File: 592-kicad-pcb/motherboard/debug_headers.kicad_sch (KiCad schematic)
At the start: 0 parts

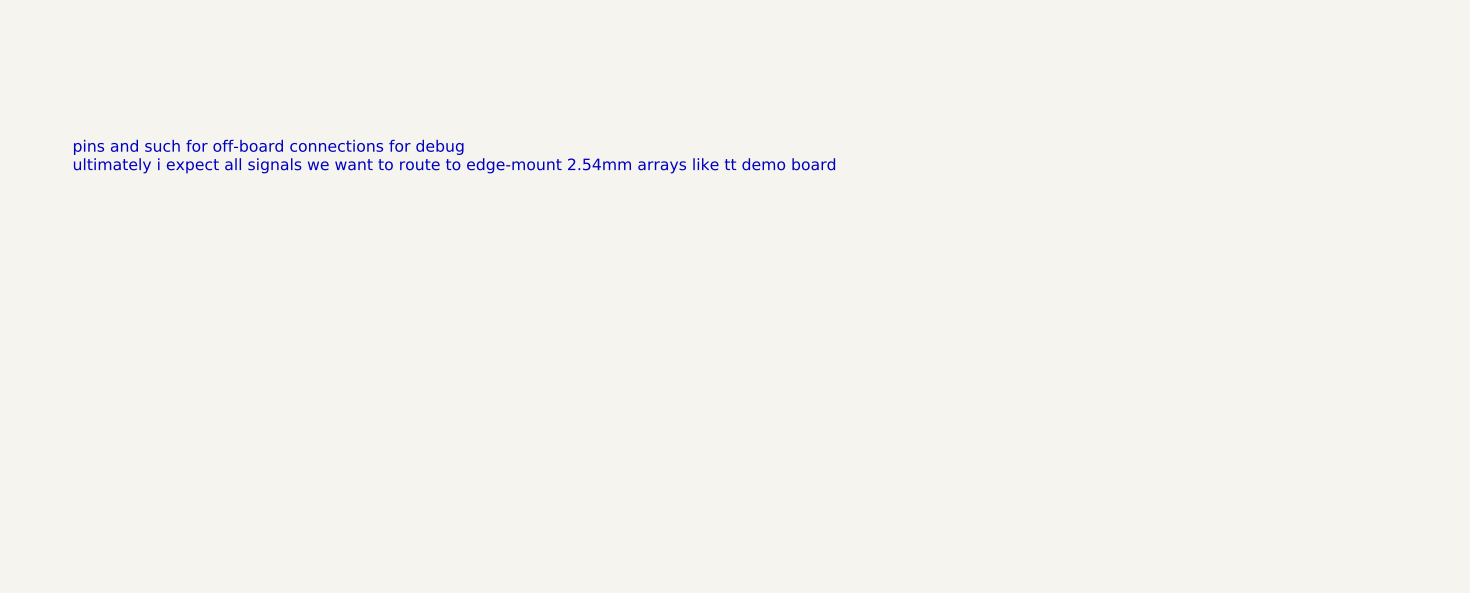
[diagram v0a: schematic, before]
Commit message: clean up supporting blocks; add nucleo symbol
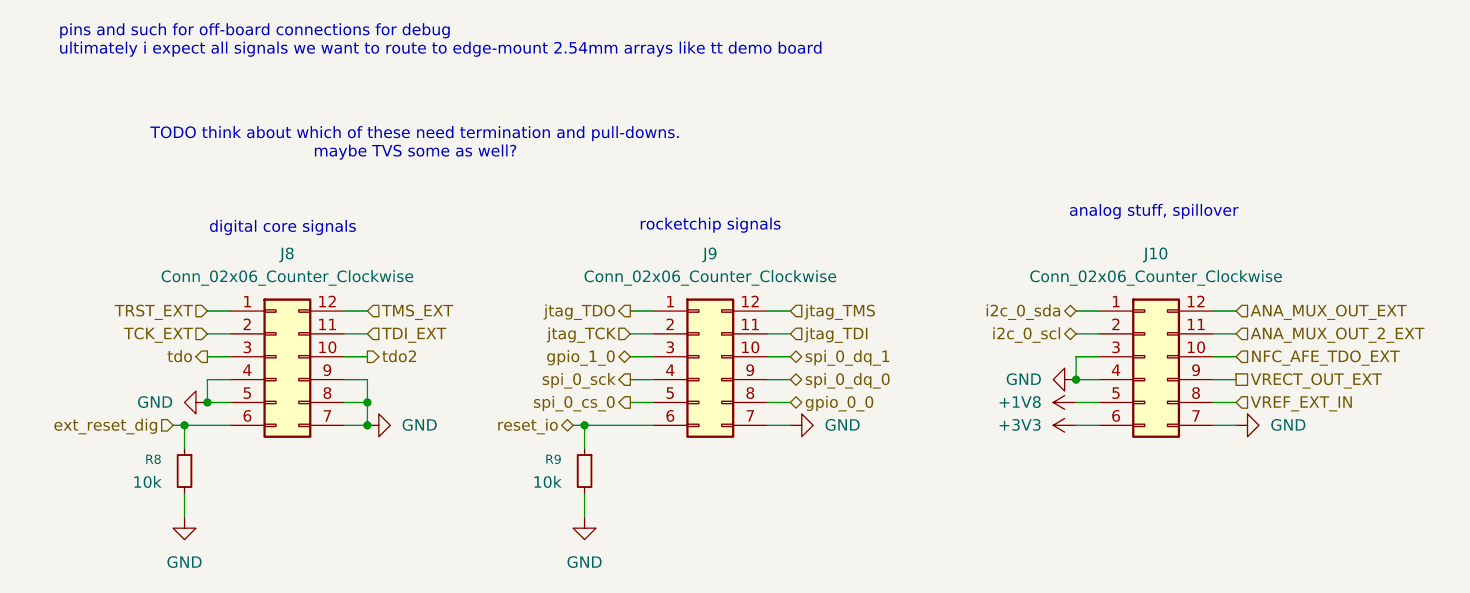
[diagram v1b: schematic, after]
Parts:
- added J10, J8, J9: Conn_02x06_Counter_Clockwise, symbol Connector_Generic:Conn_02x06_Counter_Clockwise
- added R8, R9: 10k, symbol Device:R_Small
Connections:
- new net +1V8: J10.5 (Pin_5)
- new net +3V3: J10.6 (Pin_6)
- new net ANA_MUX_OUT_2_EXT: J10.11 (Pin_11)
- new net ANA_MUX_OUT_EXT: J10.12 (Pin_12)
- new net GND: J10.3 (Pin_3), J10.4 (Pin_4), J10.7 (Pin_7), J8.4 (Pin_4), J8.5 (Pin_5), J8.7 (Pin_7), J8.8 (Pin_8), J8.9 (Pin_9), J9.7 (Pin_7), R8.2, R9.2
- new net NFC_AFE_TDO_EXT: J10.10 (Pin_10)
- new net TCK_EXT: J8.2 (Pin_2)
- new net TDI_EXT: J8.11 (Pin_11)
- new net TMS_EXT: J8.12 (Pin_12)
- new net TRST_EXT: J8.1 (Pin_1)
- new net VRECT_OUT_EXT: J10.9 (Pin_9)
- new net VREF_EXT_IN: J10.8 (Pin_8)
- new net ext_reset_dig: J8.6 (Pin_6), R8.1
- new net gpio_0_0: J9.8 (Pin_8)
- new net gpio_1_0: J9.3 (Pin_3)
- new net i2c_0_scl: J10.2 (Pin_2)
- new net i2c_0_sda: J10.1 (Pin_1)
- new net jtag_TCK: J9.2 (Pin_2)
- new net jtag_TDI: J9.11 (Pin_11)
- new net jtag_TDO: J9.1 (Pin_1)
- new net jtag_TMS: J9.12 (Pin_12)
- new net reset_io: J9.6 (Pin_6), R9.1
- new net spi_0_cs_0: J9.5 (Pin_5)
- new net spi_0_dq_0: J9.9 (Pin_9)
- new net spi_0_dq_1: J9.10 (Pin_10)
- new net spi_0_sck: J9.4 (Pin_4)
- new net tdo: J8.3 (Pin_3)
- new net tdo2: J8.10 (Pin_10)
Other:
- note added: "TODO think about which of these need termination and pull-downs. maybe TVS some as well?"
- note added: "analog stuff, spillover"
- note added: "digital core signals"
- note added: "rocketchip signals"

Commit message: add footprints for signal conditioning
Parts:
- removed J10, J8, J9: Conn_02x06_Counter_Clockwise, symbol Connector_Generic:Conn_02x06_Counter_Clockwise
- added J4, J5, J7: Conn_02x06_Odd_Even, Connector_PinSocket_2.54mm:PinSocket_2x06_P2.54mm_Horizontal, symbol Connector_Generic:Conn_02x06_Odd_Even
- R8, R9: footprint (none) -> Capacitor_SMD:C_0603_1608Metric
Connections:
- net +1V8: now also J7.9 (Pin_9)
- net +3V3: now also J7.11 (Pin_11)
- net ANA_MUX_OUT_2_EXT: now also J7.4 (Pin_4)
- net ANA_MUX_OUT_EXT: now also J7.2 (Pin_2)
- net GND: now also J4.10 (Pin_10), J4.12 (Pin_12), J4.7 (Pin_7), J4.8 (Pin_8), J4.9 (Pin_9), J5.12 (Pin_12), J7.12 (Pin_12), J7.5 (Pin_5), J7.7 (Pin_7)
- net NFC_AFE_TDO_EXT: now also J7.6 (Pin_6)
- net TCK_EXT: now also J4.3 (Pin_3)
- net TDI_EXT: now also J4.4 (Pin_4)
- net TMS_EXT: now also J4.2 (Pin_2)
- net TRST_EXT: now also J4.1 (Pin_1)
- net VRECT_OUT_EXT: now also J7.8 (Pin_8)
- net VREF_EXT_IN: now also J7.10 (Pin_10)
- net ext_reset_dig: now also J4.11 (Pin_11)
- net gpio_0_0: now also J5.10 (Pin_10)
- net gpio_1_0: now also J5.5 (Pin_5)
- net i2c_0_scl: now also J7.3 (Pin_3)
- net i2c_0_sda: now also J7.1 (Pin_1)
- net jtag_TCK: now also J5.3 (Pin_3)
- net jtag_TDI: now also J5.4 (Pin_4)
- net jtag_TDO: now also J5.1 (Pin_1)
- net jtag_TMS: now also J5.2 (Pin_2)
- net reset_io: now also J5.11 (Pin_11)
- net spi_0_cs_0: now also J5.9 (Pin_9)
- net spi_0_dq_0: now also J5.8 (Pin_8)
- net spi_0_dq_1: now also J5.6 (Pin_6)
- net spi_0_sck: now also J5.7 (Pin_7)
- net tdo: now also J4.5 (Pin_5)
- net tdo2: now also J4.6 (Pin_6)

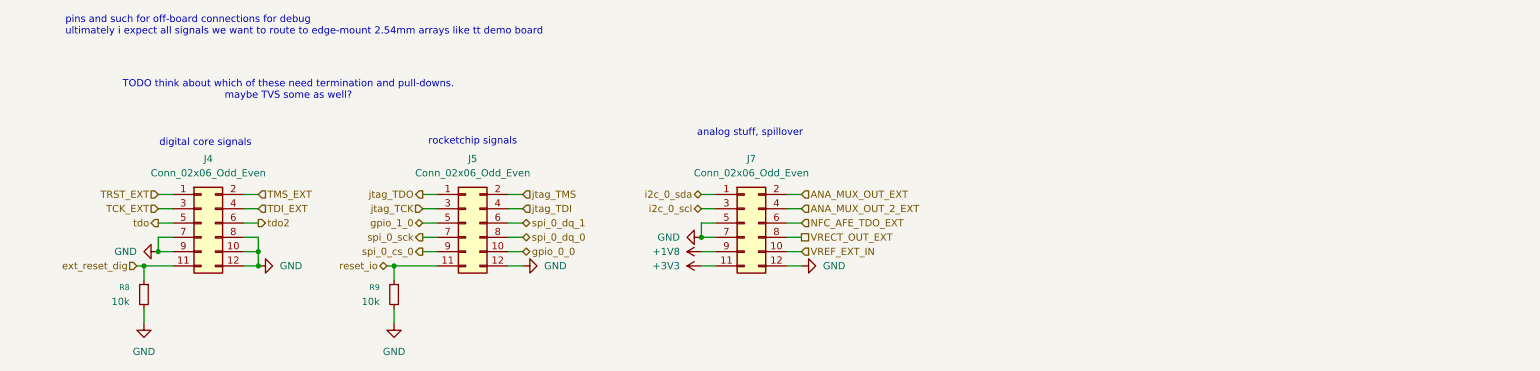
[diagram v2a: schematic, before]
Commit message: update motheboard schems to include conn
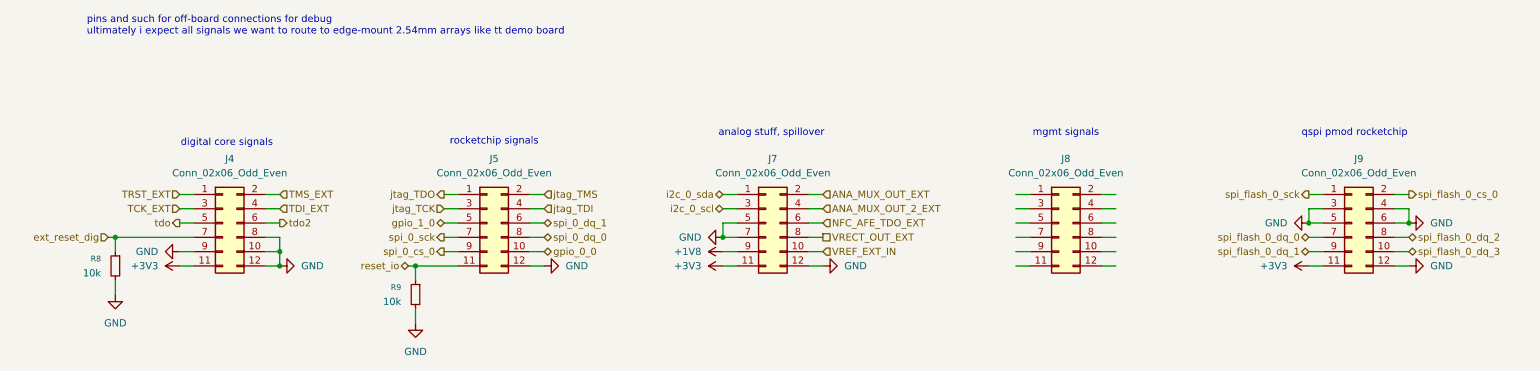
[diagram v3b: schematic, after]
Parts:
- added J8, J9: Conn_02x06_Odd_Even, Connector_PinSocket_2.54mm:PinSocket_2x06_P2.54mm_Horizontal, symbol Connector_Generic:Conn_02x06_Odd_Even
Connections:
- net +3V3: now also J4.11 (Pin_11), J9.11 (Pin_11)
- net GND: now also J9.12 (Pin_12), J9.3 (Pin_3), J9.4 (Pin_4), J9.5 (Pin_5), J9.6 (Pin_6); no longer J4.7 (Pin_7)
- net ext_reset_dig: now also J4.7 (Pin_7); no longer J4.11 (Pin_11)
- new net spi_flash_0_cs_0: J9.2 (Pin_2)
- new net spi_flash_0_dq_0: J9.7 (Pin_7)
- new net spi_flash_0_dq_1: J9.9 (Pin_9)
- new net spi_flash_0_dq_2: J9.8 (Pin_8)
- new net spi_flash_0_dq_3: J9.10 (Pin_10)
- new net spi_flash_0_sck: J9.1 (Pin_1)
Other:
- note added: "mgmt signals"
- note added: "qspi pmod rocketchip"
- note removed: "TODO think about which of these need termination and pull-downs. maybe TVS some as well?"
- moved on the sheet: J4, J5, J7, R8, R9

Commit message: in-class work at schems
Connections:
- net +3V3: now also J9.12 (Pin_12)
- net GND: now also J9.10 (Pin_10), J9.9 (Pin_9); no longer J9.12 (Pin_12), J9.3 (Pin_3), J9.4 (Pin_4), J9.5 (Pin_5), J9.6 (Pin_6)
- net spi_flash_0_dq_0: no longer J9.7 (Pin_7)
- net spi_flash_0_dq_1: no longer J9.9 (Pin_9)
- net spi_flash_0_dq_2: no longer J9.8 (Pin_8)
- net spi_flash_0_dq_3: no longer J9.10 (Pin_10)
- net spi_flash_0_sck: now also J9.8 (Pin_8); no longer J9.1 (Pin_1)
- new net CD: J9.5 (Pin_5)
- new net DAT1: J9.1 (Pin_1)
- new net DAT2: J9.3 (Pin_3)
- new net MISO: J9.6 (Pin_6)
- new net MOSI: J9.4 (Pin_4)
- no-connect marks 0 -> 3
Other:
- note added: "TODO: check w/ will to figure out mapping"
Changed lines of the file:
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@@
+		)
+	)
+	(text "TODO: check w/ will to figure out mapping"
+		(exclude_from_sim no)
+		(at 250.444 69.088 0)
+		(effects
+			(font
+				(size 1.27 1.27)
+			)
 		)
 	)
@@
 	)
 	(junction
-		(at 242.57 53.34)
-		(diameter 0)
-		(color 0 0 0 0)
-	)
-	(junction
-		(at 260.35 53.34)
-		(diameter 0)
-		(color 0 0 0 0)
-	)
-	(junction
 		(at 83.82 60.96)
 		(diameter 0)
@@
 		(color 0 0 0 0)
 	)
+	(no_connect
+		(at 242.57 50.8)
+	)
+	(no_connect
+		(at 242.57 55.88)
+	)
+	(no_connect
+		(at 242.57 48.26)
+	)
 	(wire
 		(pts
@@
 	(wire
 		(pts
-			(xy 260.35 50.8) (xy 260.35 53.34)
-		)
-		(stroke
-			(width 0)
-			(type default)
-		)
-	)
-	(wire
-		(pts
 			(xy 104.14 50.8) (xy 106.68 50.8)
 		)
@@
 		)
 	)
-	(wire
-		(pts
-			(xy 242.57 50.8) (xy 242.57 53.34)
-		)
-		(stroke
-			(width 0)
-			(type default)
+	(label "MISO"
+		(at 260.35 53.34 0)
+		(effects
+			(font
+				(size 1.27 1.27)
+			)
+			(justify left bottom)
+		)
+	)
+	(label "MOSI"
+		(at 260.35 50.8 0)
+		(effects
+			(font
+				(size 1.27 1.27)
+			)
+			(justify left bottom)
+		)
+	)
+	(label "CD"
+		(at 242.57 53.34 180)
+		(effects
+			(font
+				(size 1.27 1.27)
+			)
+			(justify right bottom)
+		)
+	)
+	(label "DAT2"
+		(at 242.57 50.8 180)
+		(effects
+			(font
+				(size 1.27 1.27)
+			)
+			(justify right bottom)
+		)
+	)
+	(label "DAT1"
+		(at 242.57 48.26 180)
+		(effects
+			(font
+				(size 1.27 1.27)
+			)
+			(justify right bottom)
 		)
 	)
@@
 	(hierarchical_label "spi_flash_0_sck"
 		(shape output)
-		(at 242.57 48.26 180)
-		(effects
-			(font
-				(size 1.27 1.27)
-			)
-			(justify right)
+		(at 260.35 55.88 0)
+		(effects
+			(font
+				(size 1.27 1.27)
+			)
+			(justify left)
 		)
 	)
 	(hierarchical_label "spi_flash_0_dq_1"
 		(shape bidirectional)
-		(at 242.57 58.42 180)
+		(at 234.95 36.83 180)
 		(effects
 			(font
@@
 	(hierarchical_label "spi_flash_0_dq_0"
 		(shape bidirectional)
-		(at 242.57 55.88 180)
+		(at 234.95 34.29 180)
 		(effects
 			(font
@@
 	(hierarchical_label "spi_flash_0_dq_2"
 		(shape bidirectional)
-		(at 260.35 55.88 0)
+		(at 283.21 46.99 0)
 		(effects
 			(font
@@
 	(hierarchical_label "spi_flash_0_dq_3"
 		(shape bidirectional)
-		(at 260.35 58.42 0)
+		(at 283.21 49.53 0)
 		(effects
 			(font
@@
 	(symbol
 		(lib_id "power:GND")
-		(at 260.35 53.34 90)
+		(at 260.35 58.42 90)
 		(unit 1)
 		(exclude_from_sim no)
@@
 		(fields_autoplaced yes)
 		(property "Reference" "#PWR080"
-			(at 266.7 53.34 0)
+			(at 266.7 58.42 0)
 			(effects
 				(font
@@
 		)
 		(property "Value" "GND"
-			(at 264.16 53.3399 90)
+			(at 264.16 58.4199 90)
 			(effects
 				(font
@@
 		)
 		(property "Footprint" ""
-			(at 260.35 53.34 0)
+			(at 260.35 58.42 0)
 			(effects
 				(font
@@
 		)
 		(property "Datasheet" ""
-			(at 260.35 53.34 0)
+			(at 260.35 58.42 0)
 			(effects
 				(font
@@
 		)
 		(property "Description" "Power symbol creates a global label with name \"GND\" , ground"
-			(at 260.35 53.34 0)
+			(at 260.35 58.42 0)
 			(effects
 				(font
@@
 	(symbol
 		(lib_id "power:+3V3")
-		(at 242.57 60.96 90)
+		(at 260.35 60.96 270)
 		(unit 1)
 		(exclude_from_sim no)
@@
 		(fields_autoplaced yes)
 		(property "Reference" "#PWR082"
-			(at 246.38 60.96 0)
+			(at 256.54 60.96 0)
 			(effects
 				(font
@@
 		)
 		(property "Value" "+3V3"
-			(at 238.76 60.9599 90)
+			(at 264.16 60.9599 90)
 			(effects
 				(font
@@
 		)
 		(property "Footprint" ""
-			(at 242.57 60.96 0)
+			(at 260.35 60.96 0)
 			(effects
 				(font
@@
 		)
 		(property "Datasheet" ""
-			(at 242.57 60.96 0)
+			(at 260.35 60.96 0)
 			(effects
 				(font
@@
 		)
 		(property "Description" "Power symbol creates a global label with name \"+3V3\""
-			(at 242.57 60.96 0)
+			(at 260.35 60.96 0)
 			(effects
 				(font
@@
 	)
 	(symbol
+		(lib_id "power:+3V3")
+		(at 242.57 60.96 90)
+		(unit 1)
+		(exclude_from_sim no)
+		(in_bom yes)
+		(on_board yes)
+		(dnp no)
+		(fields_autoplaced yes)
+		(property "Reference" "#PWR083"
+			(at 246.38 60.96 0)
+			(effects
+				(font
+					(size 1.27 1.27)
+				)
+				(hide yes)
+			)
+		)
+		(property "Value" "+3V3"
+			(at 238.76 60.9599 90)
+			(effects
+				(font
+					(size 1.27 1.27)
+				)
+				(justify left)
+			)
+		)
+		(property "Footprint" ""
+			(at 242.57 60.96 0)
+			(effects
+				(font
+					(size 1.27 1.27)
+				)
+				(hide yes)
+			)
+		)
+		(property "Datasheet" ""
+			(at 242.57 60.96 0)
+			(effects
+				(font
+					(size 1.27 1.27)
+				)
+				(hide yes)
+			)
+		)
+		(property "Description" "Power symbol creates a global label with name \"+3V3\""
+			(at 242.57 60.96 0)
+			(effects
+				(font
+					(size 1.27 1.27)
+				)
+				(hide yes)
+			)
+		)
+		(pin "1"
+		)
+		(instances
+			(project "motherboard"
+				(path "/5b0c97ac-fa03-4db8-b41b-0eee32b6f55d/d6451fe0-7223-4dc8-a216-7efc3a379119"
+					(reference "#PWR083")
+					(unit 1)
+				)
+			)
+		)
+	)
+	(symbol
 		(lib_id "Connector_Generic:Conn_02x06_Odd_Even")
 		(at 49.53 53.34 0)
@@
 	(symbol
 		(lib_id "power:GND")
-		(at 242.57 53.34 270)
+		(at 242.57 58.42 270)
 		(unit 1)
 		(exclude_from_sim no)
@@
 		(fields_autoplaced yes)
 		(property "Reference" "#PWR081"
-			(at 236.22 53.34 0)
+			(at 236.22 58.42 0)
 			(effects
 				(font
@@
 		)
 		(property "Value" "GND"
-			(at 238.76 53.3399 90)
+			(at 238.76 58.4199 90)
 			(effects
 				(font
@@
 		)
 		(property "Footprint" ""
-			(at 242.57 53.34 0)
+			(at 242.57 58.42 0)
 			(effects
 				(font
@@
 		)
 		(property "Datasheet" ""
-			(at 242.57 53.34 0)
+			(at 242.57 58.42 0)
 			(effects
 				(font
@@
 		)
 		(property "Description" "Power symbol creates a global label with name \"GND\" , ground"
-			(at 242.57 53.34 0)
+			(at 242.57 58.42 0)
 			(effects
 				(font
@@
 	(symbol
 		(lib_id "power:GND")
-		(at 260.35 60.96 90)
+		(at 283.21 52.07 90)
 		(unit 1)
 		(exclude_from_sim no)
@@
 		(fields_autoplaced yes)
 		(property "Reference" "#PWR077"
-			(at 266.7 60.96 0)
+			(at 289.56 52.07 0)
 			(effects
 				(font
@@
 		)
 		(property "Value" "GND"
-			(at 264.16 60.9599 90)
+			(at 287.02 52.0699 90)
 			(effects
 				(font
@@
 		)
 		(property "Footprint" ""
-			(at 260.35 60.96 0)
+			(at 283.21 52.07 0)
 			(effects
 				(font
@@
 		)
 		(property "Datasheet" ""
-			(at 260.35 60.96 0)
+			(at 283.21 52.07 0)
 			(effects
 				(font
@@
 		)
 		(property "Description" "Power symbol creates a global label with name \"GND\" , ground"
-			(at 260.35 60.96 0)
-			(effects
-				(font
+			(at 283.21 52.07 0)
+			(effects
+				(font
